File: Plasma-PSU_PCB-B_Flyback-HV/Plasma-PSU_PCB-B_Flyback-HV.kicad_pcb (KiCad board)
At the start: 2 copper layers, 160 x 100 mm, 30 parts, among them J101 PWM_IN, J102 PWR_IN, J103 ENBL_IN, Q101 BT169B, Q102 TIP41C, Q103 TIP42C, Q104 BT169B, Q105 IPW60, U101 L7812, U102 L7805, U103 ILD74

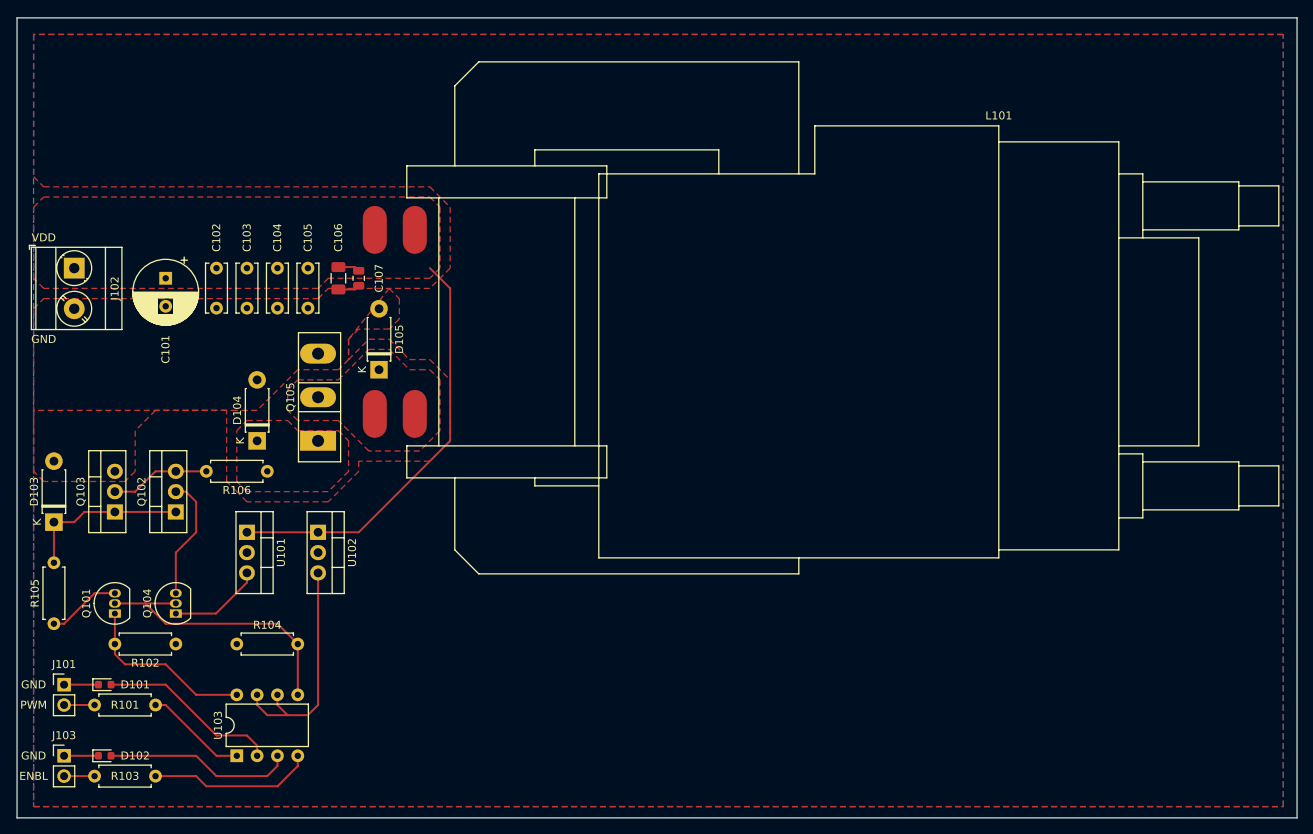
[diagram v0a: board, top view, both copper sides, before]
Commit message: Flyback PCB w/ SMD & Earth
- Changed most resistors to SMD
- Included Earth planes separate from GND for shielding
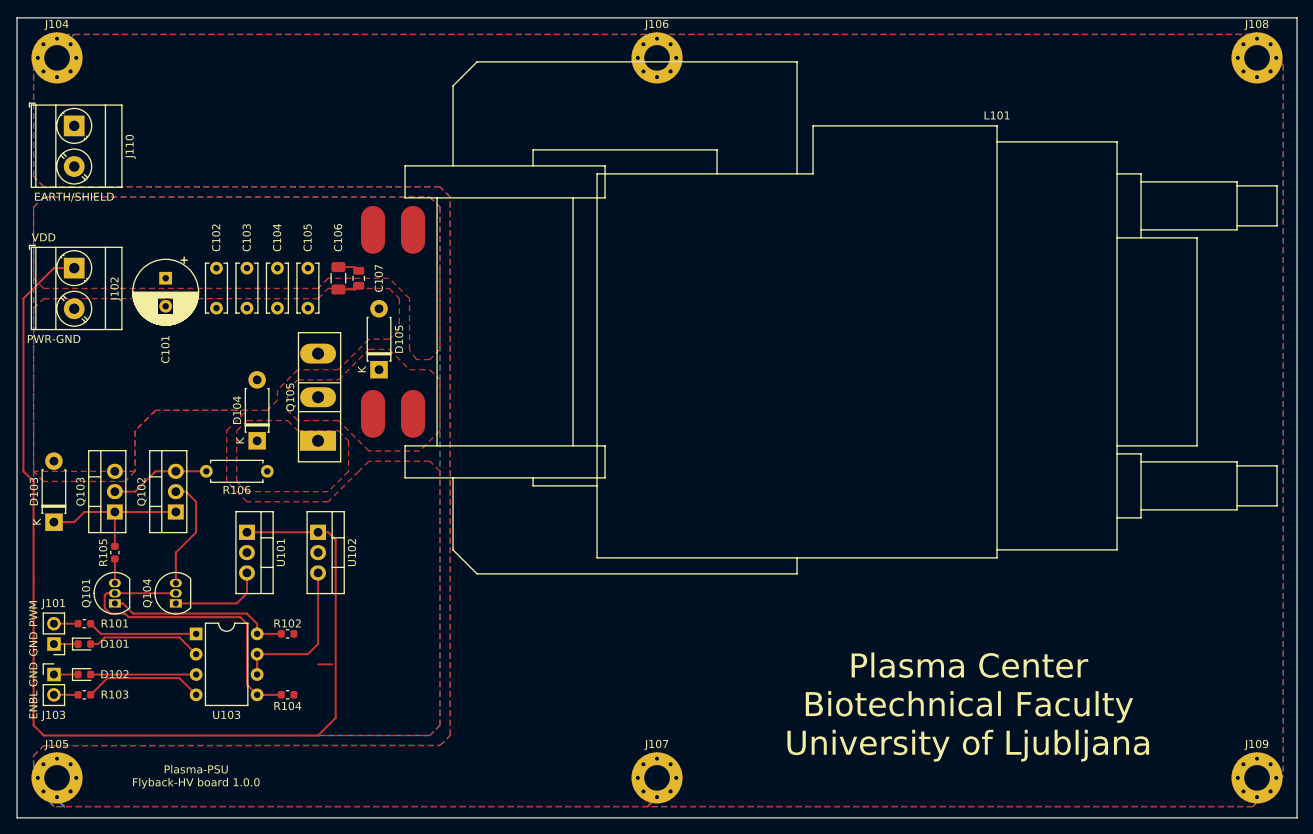
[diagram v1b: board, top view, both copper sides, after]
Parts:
- added J104: Conn_01x01_Female, MountingHole:MountingHole_3.2mm_M3_Pad_Via, F.Cu at (55.0, 55.0)
- added J105: Conn_01x01_Female, MountingHole:MountingHole_3.2mm_M3_Pad_Via, F.Cu at (55.0, 145.0)
- added J106: Conn_01x01_Female, MountingHole:MountingHole_3.2mm_M3_Pad_Via, F.Cu at (130.0, 55.0)
- added J107: Conn_01x01_Female, MountingHole:MountingHole_3.2mm_M3_Pad_Via, F.Cu at (130.0, 145.0)
- added J108: Conn_01x01_Female, MountingHole:MountingHole_3.2mm_M3_Pad_Via, F.Cu at (205.0, 55.0)
- added J109: Conn_01x01_Female, MountingHole:MountingHole_3.2mm_M3_Pad_Via, F.Cu at (205.0, 145.0)
- added J110: GND_SHIELD, TerminalBlock_Phoenix:TerminalBlock_Phoenix_MKDS-3-2-5.08_1x02_P5.08mm_Horizontal, F.Cu at (57.1, 63.5)
- R101, R102, R103, R104, R105: footprint Resistor_THT:R_Axial_DIN0207_L6.3mm_D2.5mm_P7.62mm_Horizontal -> Resistor_SMD:R_0603_1608Metric
- moved U103 16.1 mm to (72.4, 127.0), turned to 0 degrees
- moved R102 14.0 mm to (83.8, 127.0)
- moved R103 13.5 mm to (58.4, 134.6)
- moved R101 13.5 mm to (58.4, 125.7)
- moved R105 11.7 mm to (62.2, 116.8)
- moved D102 10.5 mm to (58.4, 132.1)
- moved J103 10.2 mm to (54.6, 132.1)
- moved R104 8.98 mm to (83.8, 134.6), turned to 180 degrees
- moved D101 5.68 mm to (58.4, 128.3)
- moved J101 5.24 mm to (54.6, 128.3), turned to 180 degrees
- moved Q101 1.27 mm to (62.2, 123.2)
- moved Q104 1.27 mm to (69.8, 123.2)
- moved L101 0.22 mm to (172.5, 63.5)
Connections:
- L101 pad 3: (no net) -> VDD
- L101 pad 4: (no net) -> Net-(D105-Pad1)
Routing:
- net VDD: track 55.5 -> 137.5 mm
- net Earth_Protective: track 0.00 -> 10.7 mm
- net Net-(D102-Pad2): track 23.7 -> 13.2 mm
- net +5V: track 29.5 -> 19.6 mm
- net Net-(D101-Pad2): track 22.7 -> 14.4 mm
- net Net-(Q101-Pad3): track 9.20 -> 3.02 mm
- net ENBL: track 35.1 -> 41.2 mm
- net Net-(R103-Pad1): track 20.6 -> 14.9 mm
- net GND: track 2.73 -> 4.48 mm
- net +12V: track 11.7 -> 13.2 mm
- net Net-(Q102-Pad2): track 15.5 -> 14.3 mm
- net Net-(D102-Pad1): track 4.29 -> 3.02 mm
- net Net-(D101-Pad1): track 4.29 -> 3.02 mm
- net Net-(R101-Pad1): track 12.8 -> 13.7 mm
- net Net-(D103-Pad1): track 20.8 -> 20.1 mm
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- added copper zone on B.Cu, net Earth_Protective
- added copper zone on F.Cu, net Earth_Protective
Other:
- board text added: "EARTH/SHIELD"
- board text added: "PWR-GND"
- board text added: "Plasma Center Biotechnical Faculty University of Ljubljana"
- board text added: "Plasma-PSU Flyback-HV board 1.0.0"
